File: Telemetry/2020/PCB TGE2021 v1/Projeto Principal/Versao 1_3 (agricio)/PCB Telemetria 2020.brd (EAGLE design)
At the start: 160 x 100 mm, 39 parts, among them IC1 INA240A1DR, IC2 MCP3221A6T-E_OTVAO, IC3 AZ1117IH-3.3TRG1, IC4 ACS758LCB-050B-PFF-T, IC5 ADS1115IDGSR, U2 ACS712ELCTR-05B-T

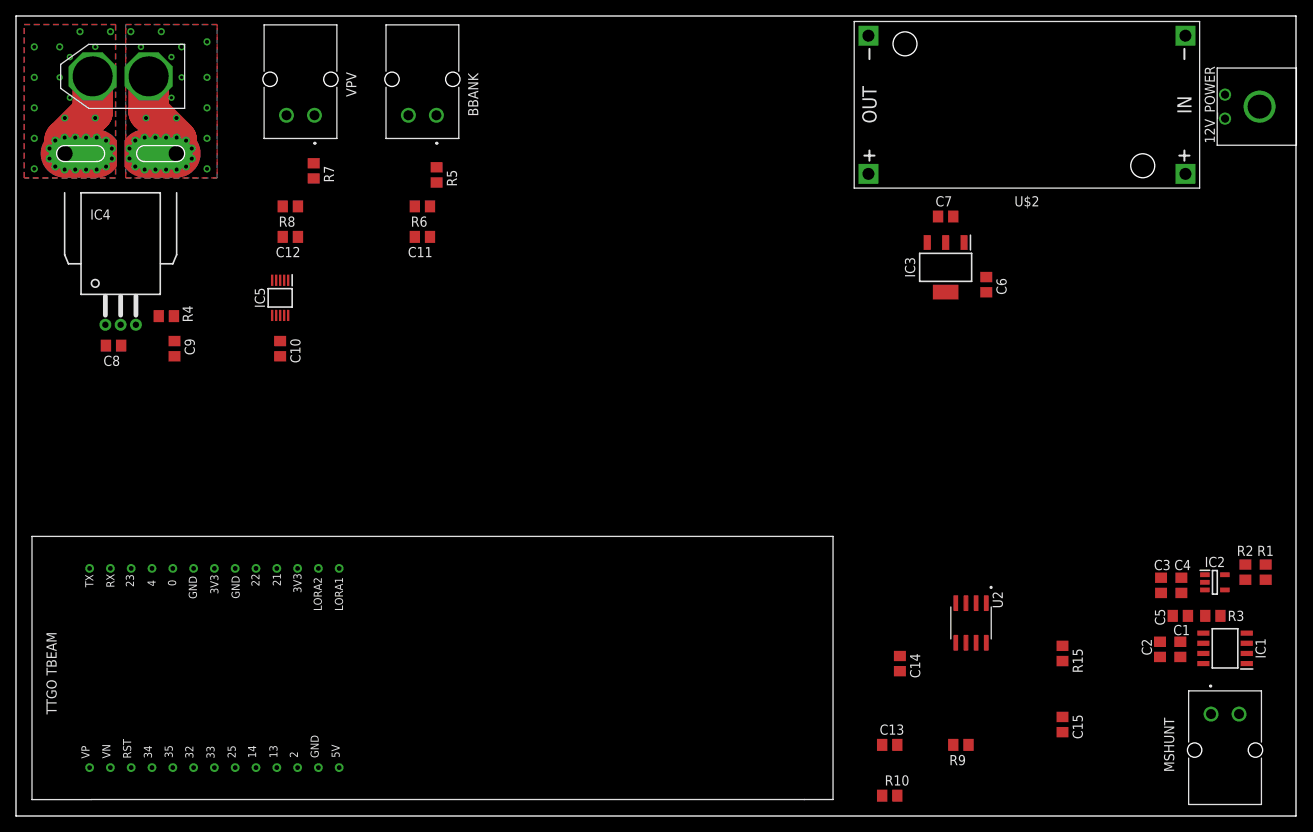
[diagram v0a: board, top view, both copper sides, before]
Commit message: Correcao no circuito de medicao de corrente, adicao de conectores e simulacao da medicao de corrente
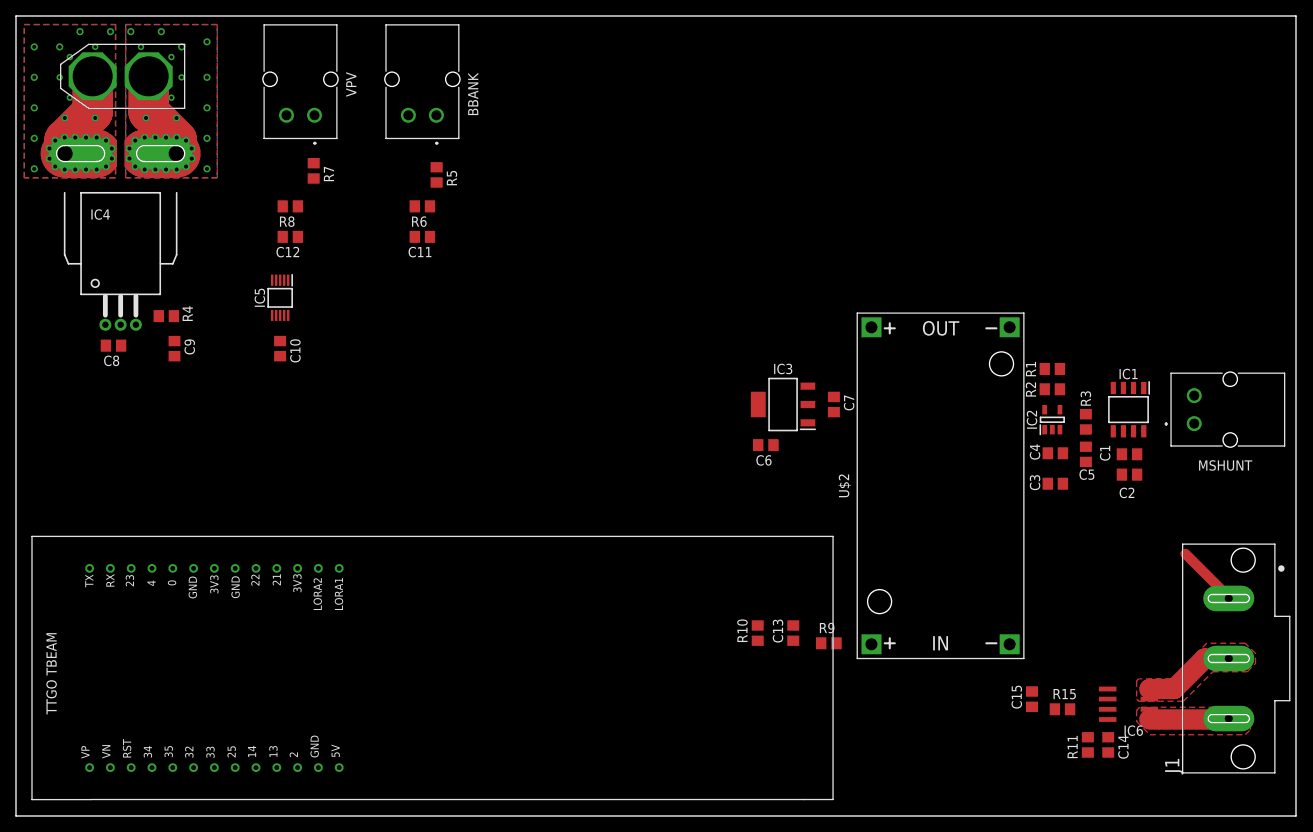
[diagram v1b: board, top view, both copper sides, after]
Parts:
- removed 12V_POWER: 43650-0200, 43650-0200:43650-0200
- removed U2: ACS712ELCTR-05B-T, ACS712ELCTR-05B-T:SOIC127P600X175-8N
- added IC6: ACS712-030B3, allegro-2:SOIC8
- added J1: 172042-0406, 172042-0302:MOLEX_172042-0406
- added R11: 4.7k, rcl:R0805
- C14: value 1nF -> 100nF
- R15: value 4.7k -> 1.6k
- moved U$2 48.8 mm to (115.6, 41.3), turned to 90 degrees
- moved MSHUNT 41.9 mm to (151.1, 50.8), turned to 90 degrees
- moved R1 36.8 mm to (129.5, 55.9), turned to 180 degrees
- moved C6 34.1 mm to (93.7, 46.4), turned to 0 degrees
- moved R2 33.2 mm to (129.5, 53.3), turned to 180 degrees
- moved IC1 32.2 mm to (139.1, 50.8), turned to 270 degrees
- moved R3 29.0 mm to (133.7, 49.3), turned to 90 degrees
- moved IC2 28.7 mm to (129.5, 49.5), turned to 90 degrees
- moved C14 27.9 mm to (136.5, 8.89)
- moved C7 27.3 mm to (102.2, 51.4), turned to 270 degrees
- moved IC3 26.6 mm to (95.9, 51.4), turned to 180 degrees
- moved R10 26.2 mm to (92.7, 22.9), turned to 90 degrees
- moved C1 25.2 mm to (139.2, 45.2), turned to 0 degrees
- moved C5 23.4 mm to (133.7, 45.2), turned to 270 degrees
- moved C4 22.8 mm to (129.9, 45.3), turned to 0 degrees
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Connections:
- removed net HS_FILTER: C14.1, U2.6
- removed net HS_OUT: R15.1, U2.7
- new net 12V_CURRENT_M: IC6.1, IC6.2, J1.3
- new net N$1: IC6.6, R11.2
- new net N$2: IC6.7, R15.1
- net GND: now also IC6.5, J1.1; no longer 12V_POWER.1, U2.3, U2.4, U2.5
- net VCC_12V: now also IC6.3, IC6.4, J1.2; no longer 12V_POWER.2, U2.1, U2.2
- net VCC_3V3: now also C14.1, IC6.8, R11.1; no longer U2.8
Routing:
- net VCC_12V: track 0.00 -> 12.8 mm
- net 12V_CURRENT_M: track 0.00 -> 11.2 mm
- net GND: track 0.00 -> 7.82 mm
- added copper zone on layer 1, net 12V_CURRENT_M
- added copper zone on layer 1, net VCC_12V
